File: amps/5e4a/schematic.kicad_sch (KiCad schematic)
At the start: 63 parts, among them T3 OT

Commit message: Add: sheet<->board net-equivalence gate over every part, no netlist (survey + drift-gated worklist)
pipeline/verify_sheet_vs_board.py proves the schematic and the board layout
draw the SAME circuit over the ~1,280 BOM passives the DC netlist does not
model — the parts both existing equivalence gates skip by construction. The
two drawings are authored independently, so their net partitions are each
other's witness: <GND>, tube pins (through basing + the datasheet unit the
sheet states), pot wipers, jack contacts (cx:JACK T/S <-> J.tip/J.sleeve)
and declared net_map.leads anchor the partitions to each other; two-terminal
parts and pot ends resolve as unordered pairs by majority voting; a
section<->unit swap is searched for on every dual-section socket and
reported once. Heaters and the pilot lamp are excluded (check_heaters owns
them); every symbol class the board cannot name is listed in scope.

Declarations (docs/layout-schema.md): a sheet part the board neither places
nor wires must be covered by net_map.netlist_unplaced / series_bridge
(layout or sch_map — a bridged part the board does not place is compared
as one net, the conductor runs through it), a new per-part
net_map.not_on_board, or a new board-scope rule scope.not_drawn
(glob + why). A declaration covering nothing is a STALE DECLARATION.
No amp declares anything yet: that is a source-read job.

schematic_lib: a draw script that states `unit=` now emits it as a hidden
symbol property, Basing_unit, so the gate reads the unit off the sheet and
not the script (the script is the fallback, and the scope line says so).
Sheets drawn without unit= are byte-identical. NOT regenerated here: the
four sheets that state a unit (5e4a, 5f6, aa764, aa764-vibro) need
`draw_<id>.py` + sync-assets before the schematic-drift step of CI passes.

Found at HEAD 07dea48 (reference/sheet-board.yaml, --export), 40 amps,
38 with findings, 36 of them with both drawings claiming verified:
  SECTION-SWAP 25 sockets on 16 sheets, SPLIT 4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
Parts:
- V3A: Basing_unit (none) -> 2
- V3B: Basing_unit (none) -> 1
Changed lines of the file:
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@@
     (in_bom yes) (on_board yes)
     (property "Reference" "V3A" (at 176.348 65.878 0) (effects (font (size 1.27 1.27)) (justify left)))
-    (property "Value" "12AX7" (at 176.348 68.278 0) (effects (font (size 1.27 1.27)) (justify left))))
+    (property "Value" "12AX7" (at 176.348 68.278 0) (effects (font (size 1.27 1.27)) (justify left)))
+    (property "Basing_unit" "2" (at 176.348 70.678 0) (effects (font (size 1.27 1.27)) hide)))
   (wire (pts (xy 154.018 72.278) (xy 159.928 72.278))
     (stroke (width 0) (type default)))
@@
     (in_bom yes) (on_board yes)
     (property "Reference" "V3B" (at 173.548 31.878 0) (effects (font (size 1.27 1.27)) (justify left)))
-    (property "Value" "12AX7" (at 173.548 34.278 0) (effects (font (size 1.27 1.27)) (justify left))))
+    (property "Value" "12AX7" (at 173.548 34.278 0) (effects (font (size 1.27 1.27)) (justify left)))
+    (property "Basing_unit" "1" (at 173.548 36.678 0) (effects (font (size 1.27 1.27)) hide)))
   (wire (pts (xy 167.548 64.658) (xy 167.548 61.178))
     (stroke (width 0) (type default)))

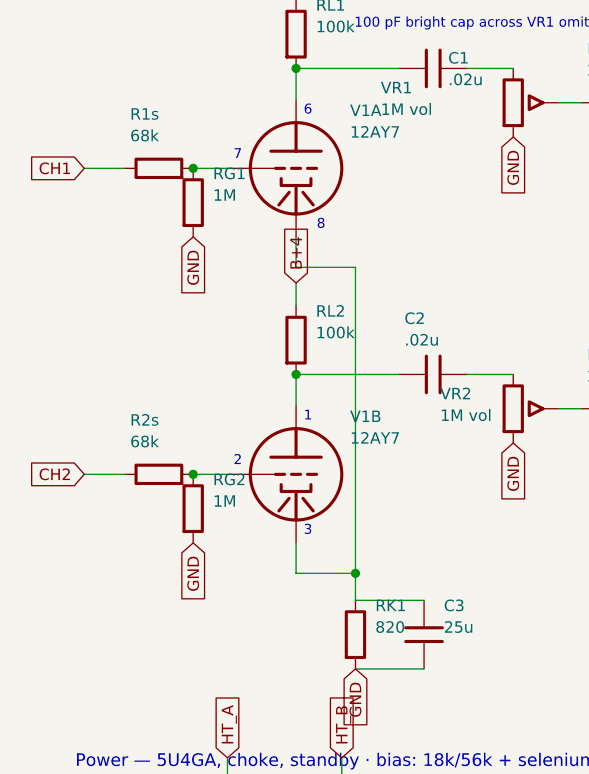
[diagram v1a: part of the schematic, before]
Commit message: Fix: draw the 1 MΩ input grid leak on the jack-1 tip node, not the grid, on eight tweed/Champ sheets
Every tweed and Champ factory sheet hangs the 1 MΩ from the jack-1 tip
node (the node the jack-2 shorting contact also lands on) to ground, and
runs the 68 K stoppers from the jack tips to the grid. These eight sheets
drew the 1 MΩ on the GRID side of the stopper — one copy-pasted idiom in
four scripts and its cousins in four more; there is no shared helper, so
each script is fixed where it draws the block. The stopper is declared
DC-transparent (layout net_map.series_bridge), so the netlist sees one node
either way and verify_schematic_nets stays 40 clean; the sheet-vs-board
gate, which compares the drawings to each other, drops all twelve
MISPLACED findings (RG1/RG2 on 5e4a, 5e5a, 5f4, 5f6; R3 on 5f2a, aa764,
aa764-vibro; R1 on 5f1). 5f10's jack chain is a separate task.

Crops read: 5e4a-RG1-RG2-input.png, 5e5a-RG1-RG2-input.png,
5f4-RG1-input.png, 5f6-RG1-RG2-input.png, 5f2a-R3-input.png,
5f1-R1-input.png, aa764-R3-input.png, aa764-vibro-R3-input.png — each
prints "1 MEG." from the jack-1 tip to ground with the 68K pair to the grid.

Geometry: the four two-channel sheets hang the leak from the stopper's
jack-side pin; 5f1 drops it from the INPUT line; 5f2a and the two Champs
stand it upward off the jack-1 line because the jack-2 line runs 8–12 mm
below. Previews read cleanly. The circuit stories already say the leaks
mount at the jacks, so no prose changed.

Gates: check_schematics 40/0 (0 isolated), verify_schematic_nets 40
clean, validate/value-consistency/era-values clean, regenerate-all leaves
every other sheet byte-identical. verify_sheet_vs_board misplaced 98 -> 86.

Co-Authored-By: Claude Fable 5.1 <noreply@anthropic.com>
Claude-Session: https://claude.ai/code/session_01KBMfdh37HmCL2iWcBiL5J1
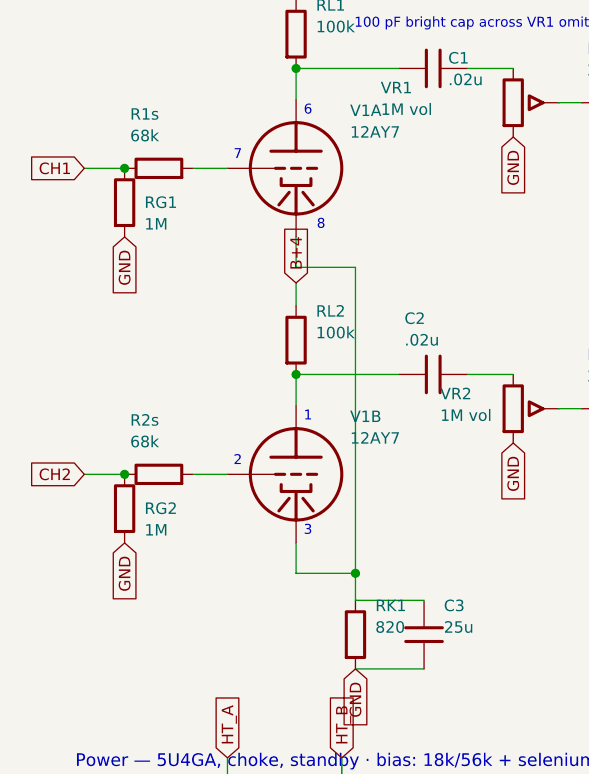
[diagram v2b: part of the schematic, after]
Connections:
- net CH1: now also RG1.1
- net CH2: now also RG2.1
- net at R1s.2, V1A.2 (G): no longer RG1.1
- net at R2s.2, V1B.2 (G): no longer RG2.1
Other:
- moved on the sheet: RG1, RG2
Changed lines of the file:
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@@
   (wire (pts (xy 29.118 38.278) (xy 32.928 38.278))
     (stroke (width 0) (type default)))
-  (junction (at 29.118 38.278) (diameter 1.013) (color 0 0 0 0))
-  (symbol (lib_id "cx:R") (at 29.118 42.088 0) (unit 1)
+  (junction (at 21.498 38.278) (diameter 1.013) (color 0 0 0 0))
+  (symbol (lib_id "cx:R") (at 21.498 42.088 0) (unit 1)
     (in_bom yes) (on_board yes)
-    (property "Reference" "RG1" (at 31.318 38.888 0) (effects (font (size 1.27 1.27)) (justify left)))
-    (property "Value" "1M" (at 31.318 41.288 0) (effects (font (size 1.27 1.27)) (justify left))))
-  (global_label "GND" (shape input) (at 29.118 45.898 270)
+    (property "Reference" "RG1" (at 23.698 42.088 0) (effects (font (size 1.27 1.27)) (justify left)))
+    (property "Value" "1M" (at 23.698 44.488 0) (effects (font (size 1.27 1.27)) (justify left))))
+  (global_label "GND" (shape input) (at 21.498 45.898 270)
     (effects (font (size 1.27 1.27)) (justify right)))
   (wire (pts (xy 40.548 30.658) (xy 40.548 27.178))
@@
   (wire (pts (xy 29.118 72.278) (xy 32.928 72.278))
     (stroke (width 0) (type default)))
-  (junction (at 29.118 72.278) (diameter 1.013) (color 0 0 0 0))
-  (symbol (lib_id "cx:R") (at 29.118 76.088 0) (unit 1)
+  (junction (at 21.498 72.278) (diameter 1.013) (color 0 0 0 0))
+  (symbol (lib_id "cx:R") (at 21.498 76.088 0) (unit 1)
     (in_bom yes) (on_board yes)
-    (property "Reference" "RG2" (at 31.318 72.888 0) (effects (font (size 1.27 1.27)) (justify left)))
-    (property "Value" "1M" (at 31.318 75.288 0) (effects (font (size 1.27 1.27)) (justify left))))
-  (global_label "GND" (shape input) (at 29.118 79.898 270)
+    (property "Reference" "RG2" (at 23.698 76.088 0) (effects (font (size 1.27 1.27)) (justify left)))
+    (property "Value" "1M" (at 23.698 78.488 0) (effects (font (size 1.27 1.27)) (justify left))))
+  (global_label "GND" (shape input) (at 21.498 79.898 270)
     (effects (font (size 1.27 1.27)) (justify right)))
   (wire (pts (xy 40.548 64.658) (xy 40.548 61.178))

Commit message: Fix: feed the tweed bias rectifiers from the transformer's bias tap, not a rectifier plate (5E4-A, 5E5-A, 5F4, 5G9)
The 8087-family power transformer brings out a BIAS TAP on the HT winding,
between one end and the centre tap — the layouts letter that lead RED-BLUE
— and every fixed-bias tweed factory sheet draws the bias rectifier from
that fourth winding terminal. These four sheets drew it from a rectifier
plate (the HT_B label). The boards carry the same mistake, which is why the
sheet-vs-board gate could not see it; the source read did.

cx:PT gains an OPTIONAL pin 6, HT_TAP, between HT_A and the centre tap.
`s.pt(..., tap=True)` asks for it, and only that sheet's embedded library
carries the pin (lib_text(pt_tap=...)), so every sheet that does not wire
it is byte-identical — proved by the regenerate-all diff below. The
contract tables (SYM_EXTENTS/SYM_PINS) are built with the pin so the lint
and the wire-cutting know it; the tap lies inside the symbol's box, so no
extent moves.

- 5g9: T1 8160 drawn with the tap (moved 8 mm left for the label), the
  selenium rectifier's AC side on HT_TAP (crop 5g9-D1-schem.png: the
  rectifier + runs straight to a winding terminal between the 300 V AC end
  and the centre tap; layout: a separate lead to SEL. RECT. +).
- 5e4a, 5f4: these sheets drew no PT at all, so a T1 is added (MAINS labels
  on the primary, HT_A / HT_TAP / centre tap / HT_B on the secondary, the
  same idiom the 5G9 uses), the 18k / 6800 bias feed taken from HT_TAP,
  and T1 added to bom.yaml (crops 5e4a-D1-schem.png, 5f4-D1-schem.png:
  the series resistor from a winding terminal between the top end and the
  centre tap; 5e4a-D1-layout.png: RED-BLUE lead to the selenium +).
- 5e5a: T1 added the same way; the bias row now carries the factory's 10 K
  in series from the tap into the cell and the 56 K bleeder across the
  100 µF can (crop 5e5a-D1-schem.png), both added to bom.yaml (RB1, RB2)
  — the board places neither, so they report SHEET-ONLY until it doe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
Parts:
- added T1: PT, symbol cx:PT
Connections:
- net GND: now also T1.4 (HT_CT)
- net HT_A: now also T1.3 (HT_A)
- net HT_B: now also T1.5 (HT_B); no longer D1.1 (A)
- new net HT_TAP: D1.1 (A), T1.6 (HT_TAP)
- new net MAINS: T1.1 (PRI_1), T1.2 (PRI_2)
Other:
- note added: "Heaters, mains switch, fuse and standby omitted — see the netlist and the sources list"
- note removed: "Heaters, PT primary and standby omitted — see the netlist and the sources list"
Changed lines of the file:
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@@
   (global_label "GND" (shape input) (at 133.258 131.698 270)
     (effects (font (size 1.27 1.27)) (justify right)))
-  (global_label "HT_B" (shape input) (at 141.118 106.998 180)
+  (global_label "HT_TAP" (shape input) (at 141.118 106.998 180)
     (effects (font (size 1.27 1.27)) (justify right)))
   (wire (pts (xy 141.118 106.998) (xy 144.928 106.998))
@@
     (effects (font (size 1.27 1.27)) (justify right)))
   (global_label "-32V" (shape input) (at 174.138 106.998 0)
+    (effects (font (size 1.27 1.27)) (justify left)))
+  (symbol (lib_id "cx:PT") (at 196.018 122.278 0) (unit 1)
+    (in_bom yes) (on_board yes)
+    (property "Reference" "T1" (at 189.668 110.378 0) (effects (font (size 1.27 1.27)) (justify left)))
+    (property "Value" "PT" (at 189.668 112.778 0) (effects (font (size 1.27 1.27)) (justify left))))
+  (wire (pts (xy 187.128 117.198) (xy 183.128 117.198))
+    (stroke (width 0) (type default)))
+  (global_label "MAINS" (shape input) (at 183.128 117.198 180)
+    (effects (font (size 1.27 1.27)) (justify right)))
+  (wire (pts (xy 187.128 127.358) (xy 183.128 127.358))
+    (stroke (width 0) (type default)))
+  (global_label "MAINS" (shape input) (at 183.128 127.358 180)
+    (effects (font (size 1.27 1.27)) (justify right)))
+  (wire (pts (xy 204.908 117.198) (xy 216.908 117.198))
+    (stroke (width 0) (type default)))
+  (global_label "HT_A" (shape input) (at 216.908 117.198 0)
+    (effects (font (size 1.27 1.27)) (justify left)))
+  (wire (pts (xy 204.908 119.738) (xy 206.908 119.738))
+    (stroke (width 0) (type default)))
+  (global_label "HT_TAP" (shape input) (at 206.908 119.738 0)
+    (effects (font (size 1.27 1.27)) (justify left)))
+  (wire (pts (xy 204.908 122.278) (xy 216.908 122.278))
+    (stroke (width 0) (type default)))
+  (global_label "GND" (shape input) (at 216.908 122.278 0)
+    (effects (font (size 1.27 1.27)) (justify left)))
+  (wire (pts (xy 204.908 127.358) (xy 208.908 127.358))
+    (stroke (width 0) (type default)))
+  (global_label "HT_B" (shape input) (at 208.908 127.358 0)
     (effects (font (size 1.27 1.27)) (justify left)))
   (polyline (pts (xy 45.628 108.978) (xy 46.619 109.076) (xy 47.572 109.365) (xy 48.45 109.834) (xy 49.22 110.466) (xy 49.852 111.236) (xy 50.321 112.114) (xy 50.61 113.067) (xy 50.708 114.058) (xy 50.61 115.049) (xy 50.321 116.002) (xy 49.852 116.88) (xy 49.22 117.65) (xy 48.45 118.282) (xy 47.572 118.751) (xy 46.619 119.04) (xy 45.628 119.138) (xy 32.928 119.138) (xy 31.937 119.04) (xy 30.984 118.751) (xy 30.106 118.282) (xy 29.336 117.65) (xy 28.704 116.88) (xy 28.235 116.002) (xy 27.946 115.049) (xy 27.848 114.058) (xy 27.946 113.067) (xy 28.235 112.114) (xy 28.704 111.236) (xy 29.336 110.466) (xy 30.106 109.834) (xy 30.984 109.365) (xy 31.937 109.076) (xy 32.928 108.978) (xy 45.628 108.978))
@@
   (text "56k NFB from the speaker + 5k presence (0.1 µF on its wiper) land on V3A's cathode (annotation)" (at 12.7 142.856 0)
     (effects (font (size 1.2 1.2)) (justify left)))
-  (text "Heaters, PT primary and standby omitted — see the netlist and the sources list" (at 12.7 147.256 0)
+  (text "Heaters, mains switch, fuse and standby omitted — see the netlist and the sources list" (at 12.7 147.256 0)
     (effects (font (size 1.2 1.2)) (justify left)))
   (sheet_instances (path "/" (page "1")))

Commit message: Fix: six sheets letter valve sections and bias rows the way their factory drawings do
Sections — the board was right and the sheet printed the other half's pin
numbers (triage verdict rows, crops under the triage scratch):
  AC30 V1    JMI OS/065 (3600x2492): Brilliant grid 2 / plate 1, Normal 7 / 6
  AA964 V1   input 2/1/3, second stage 7/6/8 (6322x3926)
  AA964 V2   phase inverter 7/6/8, tremolo oscillator 2/1/3
  5F6-A V3   the 82k (input) triode on 1/2/3 on the I-EG layout (6402x3641)
  6G4 V5     the 82k triode on 1/2/3 on the A-FJ layout (2250x1269, the only copy)

Bias rows — the 5F4 (C-EG) and 5E4-A (G-EE) drawings run the series
resistor (6800 / 18K) from the transformer's bias tap INTO the selenium
rectifier. The previous commit's rows put the rectifier on the tap and the
resistor after it; both now read tap -> resistor -> rectifier -> node. The
5F4 rectifier sits clear of C17's ground flag.

Worklist after re-export: section swaps 10 -> 5 (three board re-pins in
flight, the 5E5-A whose only copy does not resolve, and the AA1164 V4 still
being read); the 5F4/5E4-A D1 rows stay MISPLACED until their boards take
the tap lead, which the board repair wave is adding.

Gates: check_schematics 40/0 (+selftest), verify_schematic_nets 40 clean,
tone gate, validate, check_value_consistency --strict 0, test_era_values,
verify_sheet_vs_board selftest 19 + drift clean after --export,
check_heaters, verify_layout_nets; regenerating every sheet changes only
these six.

Co-Authored-By: Claude Opus 5 (1M context) <noreply@anthropic.com>
Claude-Session: https://claude.ai/code/session_01KBMfdh37HmCL2iWcBiL5J1
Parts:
- removed D1: SEL, symbol cx:DIODE_SS
- added RB1: 18k, symbol cx:R
- D1: renamed from RB1; value 18k -> SEL; symbol cx:R -> cx:DIODE_SS
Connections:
- net HT_TAP: now also RB1.1
- net at D1.1 (A): now also RB1.2
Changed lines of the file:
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@@
   (global_label "HT_TAP" (shape input) (at 141.118 106.998 180)
     (effects (font (size 1.27 1.27)) (justify right)))
-  (wire (pts (xy 141.118 106.998) (xy 144.928 106.998))
+  (symbol (lib_id "cx:R") (at 146.018 106.998 90) (unit 1)
+    (in_bom yes) (on_board yes)
+    (property "Reference" "RB1" (at 142.818 100.998 270) (effects (font (size 1.27 1.27)) (justify left)))
+    (property "Value" "18k" (at 142.818 103.398 270) (effects (font (size 1.27 1.27)) (justify left))))
+  (wire (pts (xy 141.118 106.998) (xy 142.208 106.998))
     (stroke (width 0) (type default)))
-  (symbol (lib_id "cx:DIODE_SS") (at 150.008 106.998 0) (unit 1)
+  (wire (pts (xy 149.828 106.998) (xy 152.938 106.998))
+    (stroke (width 0) (type default)))
+  (symbol (lib_id "cx:DIODE_SS") (at 158.018 106.998 0) (unit 1)
     (in_bom yes) (on_board yes)
-    (property "Reference" "D1" (at 148.008 101.598 0) (effects (font (size 1.27 1.27)) (justify left)))
-    (property "Value" "SEL" (at 148.008 103.998 0) (effects (font (size 1.27 1.27)) (justify left))))
-  (wire (pts (xy 155.088 106.998) (xy 158.898 106.998))
-    (stroke (width 0) (type default)))
-  (symbol (lib_id "cx:R") (at 162.708 106.998 90) (unit 1)
-    (in_bom yes) (on_board yes)
-    (property "Reference" "RB1" (at 159.508 100.998 270) (effects (font (size 1.27 1.27)) (justify left)))
-    (property "Value" "18k" (at 159.508 103.398 270) (effects (font (size 1.27 1.27)) (justify left))))
-  (wire (pts (xy 158.898 106.998) (xy 158.898 106.998))
-    (stroke (width 0) (type default)))
-  (wire (pts (xy 166.518 106.998) (xy 169.058 106.998))
+    (property "Reference" "D1" (at 156.018 111.598 0) (effects (font (size 1.27 1.27)) (justify left)))
+    (property "Value" "SEL" (at 156.018 113.998 0) (effects (font (size 1.27 1.27)) (justify left))))
+  (wire (pts (xy 163.098 106.998) (xy 169.058 106.998))
     (stroke (width 0) (type default)))
   (wire (pts (xy 169.058 106.998) (xy 171.598 106.998))
